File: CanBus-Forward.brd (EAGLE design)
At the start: 19 x 14 mm, 1 part

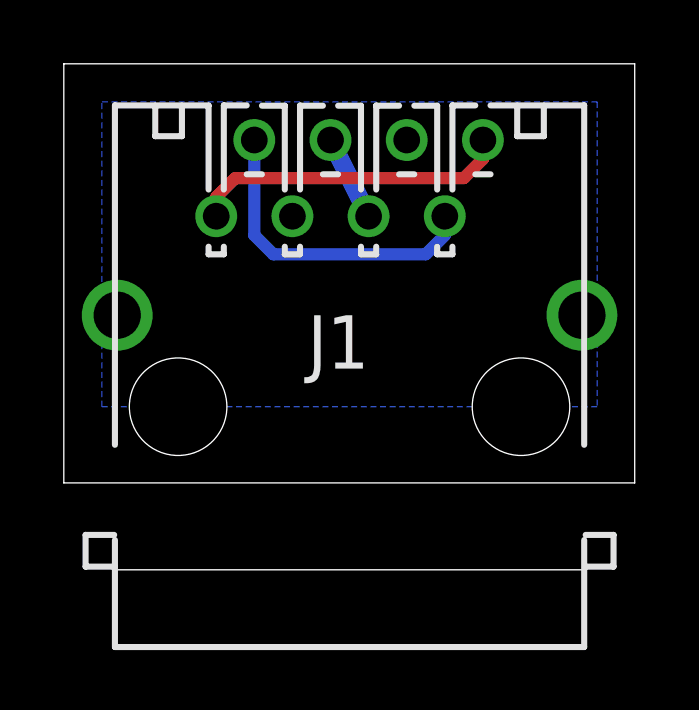
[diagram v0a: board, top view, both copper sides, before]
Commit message: CAN-Bus Beadboard-Adapter, Layouts angepasst
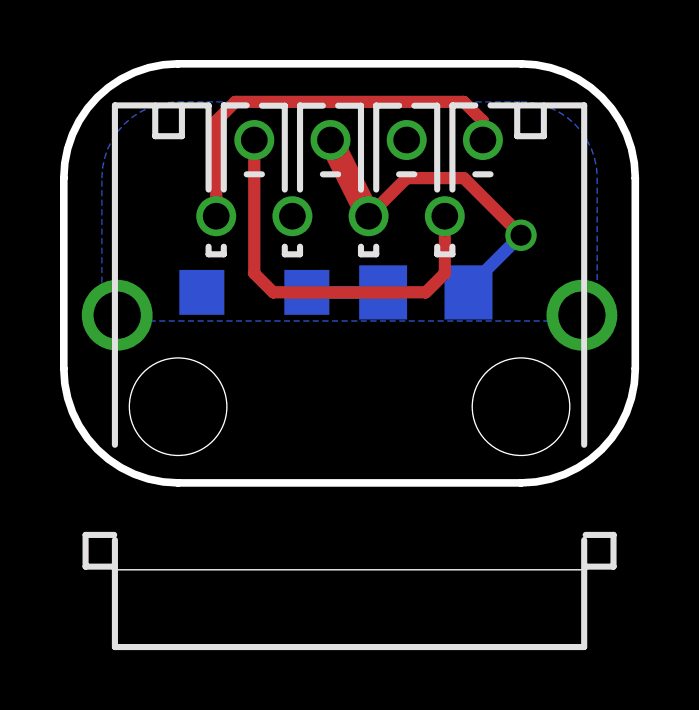
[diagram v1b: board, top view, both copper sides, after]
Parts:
- added LED1: (no value), led:CHIPLED_1206
- added R1: 1k2, rcl:R1206
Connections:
- new net N$2: LED1.A, R1.1
- net +24V: now also R1.2
- net GND: now also LED1.C
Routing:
- net +24V: track 2.84 -> 11.9 mm, vias 0 -> 1
- net N$2: track 0.00 -> 2.54 mm
- net CANL: track 10.7 -> 13.2 mm
- net CANH: track 10.7 -> 13.2 mm
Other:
- board size 19 x 14 mm -> 19.1 x 14 mm
- board text added: "CAN-Bus Weiter- leitung"
- board text removed: "CAN-Bus Weiterleitung"
